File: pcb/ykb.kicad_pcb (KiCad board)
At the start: 2 copper layers, 299.2 x 132.3 mm, 90 parts, among them J1 Conn_01x08_Socket, U1 Helios

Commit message: column trace highway
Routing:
- net col 0: track 95.2 -> 348.7 mm, vias 0 -> 4
- net col 1: track 97.9 -> 297.7 mm, vias 0 -> 4
- net row 0: track 310.3 -> 494.5 mm, vias 20 -> 22
- net col 2: track 96.7 -> 268.2 mm, vias 0 -> 4
- net col 3: track 94.4 -> 230.1 mm, vias 0 -> 4
- net col 4: track 90.5 -> 211.8 mm, vias 0 -> 4
- net col 5: track 86.8 -> 202.0 mm, vias 0 -> 4
- net row 3: track 395.1 -> 338.4 mm, vias 4 -> 2
- net Net-(D21-A): track 0.00 -> 7.78 mm
- net Net-(D22-A): track 0.00 -> 7.68 mm
- net col 6: track 121.8 -> 115.5 mm
- net col 7: track 87.1 -> 81.6 mm
- net col 8: track 89.1 -> 84.9 mm
- net col 9: track 91.3 -> 88.4 mm
- net col 10: track 93.6 -> 91.9 mm

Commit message: fixed incorrect net assignment
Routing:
- net col 11: track 95.0 -> 221.6 mm, vias 0 -> 2
- net col 0: track 348.7 -> 222.1 mm, vias 4 -> 2
- net col 10: track 91.9 -> 193.6 mm, vias 0 -> 2
- net col 1: track 297.7 -> 196.0 mm, vias 4 -> 2
- net col 9: track 88.4 -> 176.5 mm, vias 0 -> 2
- net col 2: track 268.2 -> 180.0 mm, vias 4 -> 2
- net col 3: track 230.1 -> 158.4 mm, vias 4 -> 2
- net col 8: track 84.9 -> 156.6 mm, vias 0 -> 2
- net col 7: track 81.6 -> 135.7 mm, vias 0 -> 2
- net col 4: track 211.8 -> 157.7 mm, vias 4 -> 2
- net col 6: vias 0 -> 1
- net col 5: vias 4 -> 3

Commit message: finished routing
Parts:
- moved D32 4.43 mm to (309.6, 158.7)
- moved J1 2.81 mm to (245.7, 193.2)
- moved U1 1.99 mm to (236.8, 165.9)
- moved S32 1.99 mm to (313.2, 150.0)
- moved D37 1.99 mm to (277.8, 148.9)
- moved S20 1.99 mm to (150.4, 181.2)
- moved D33 1.99 mm to (300.0, 145.0)
- moved D42 1.99 mm to (319.3, 190.4)
- moved S42 1.99 mm to (323.2, 181.2)
- moved D19 1.99 mm to (207.8, 192.9)
- moved S36 1.99 mm to (291.7, 153.1)
- moved S27 1.99 mm to (350.2, 133.9)
- moved D28 1.99 mm to (339.3, 123.9)
- moved D29 1.99 mm to (326.8, 154.4)
- moved D12 1.99 mm to (182.8, 129.4)
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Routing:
- net row 2: track 227.9 -> 544.3 mm, vias 3 -> 24
- net row 1: track 438.2 -> 624.7 mm, vias 23 -> 27
- net row 0: track 494.5 -> 675.0 mm, vias 22 -> 23
- net row 3: track 338.4 -> 513.5 mm, vias 2 -> 6
- net col 8: track 156.6 -> 259.0 mm, vias 2 -> 3
- net col 7: track 135.7 -> 232.5 mm, vias 2 -> 3
- net col 9: track 176.5 -> 271.9 mm, vias 2 -> 3
- net col 3: track 158.4 -> 252.8 mm, vias 2 -> 3
- net col 6: track 115.5 -> 207.3 mm, vias 1 -> 3
- net col 2: track 180.0 -> 270.5 mm, vias 2 -> 3
- net col 4: track 157.7 -> 237.4 mm, vias 2 -> 4
- net col 1: track 196.0 -> 261.9 mm, vias 2 -> 3
- net col 10: track 193.6 -> 256.9 mm, vias 2 -> 3
- net col 11: track 221.6 -> 271.5 mm, vias 2 -> 3
- net col 0: track 222.1 -> 272.0 mm, vias 2 -> 3
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
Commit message: all done other than mounting holes :3
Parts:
- J1: value Conn_01x08_Socket -> Conn_01x07_Socket; footprint Connector_PinHeader_2.54mm:PinHeader_1x08_P2.54mm_Vertical -> Connector_PinHeader_2.54mm:PinHeader_1x07_P2.54mm_Vertical
- moved J1 5.51 mm to (244.5, 198.6)
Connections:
- U1 pad 34: DBL -> unconnected-(U1-P25-Pad34)
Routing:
- net row 2: track 544.3 -> 583.2 mm, vias 24 -> 23
- net DBL: track 17.5 -> 0.00 mm
- net row 1: track 624.7 -> 615.0 mm
- net DDC: track 12.6 -> 18.8 mm
- net DCLK: track 12.6 -> 18.4 mm
- net DDIN: track 12.6 -> 18.4 mm
- net DRST: track 12.6 -> 18.4 mm
- net DCS: track 12.6 -> 18.4 mm
- net 3v3: track 38.8 -> 43.1 mm
- net gnd: track 44.7 -> 49.1 mm
- net col 5: track 206.6 -> 208.2 mm
- net col 1: track 261.9 -> 261.1 mm
- net col 10: track 256.9 -> 256.2 mm
- net col 2: track 270.5 -> 270.0 mm
- net col 4: vias 4 -> 3

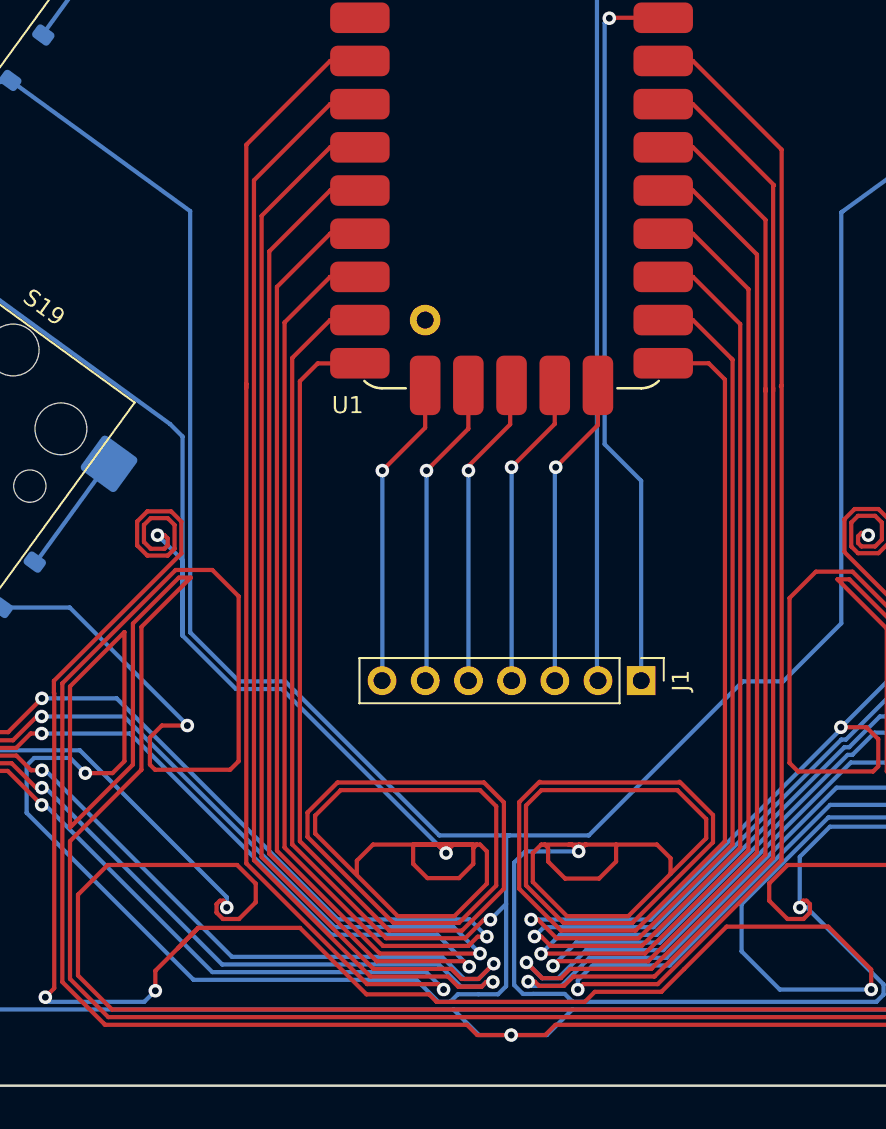
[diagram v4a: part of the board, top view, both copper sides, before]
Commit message: fixed lcd and some design rule errors
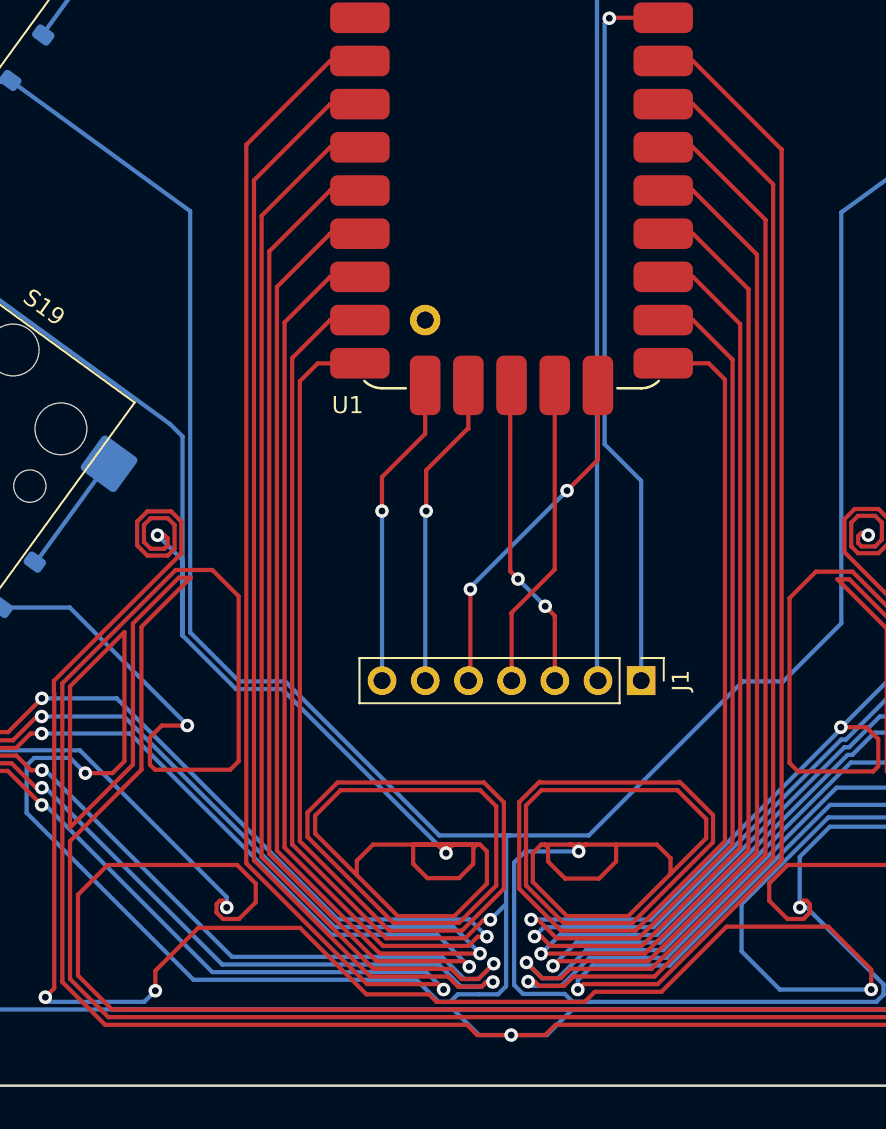
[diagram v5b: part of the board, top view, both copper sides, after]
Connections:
- net DCLK renamed DSDA
- J1 pad 3: DDIN -> DSCL
- J1 pad 5: DCS -> DDC
- J1 pad 6: DDC -> DCS
- U1 pad 26: DDC -> DCS
- U1 pad 27: DCS -> DSCL
- U1 pad 29: DDIN -> DDC
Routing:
- net DSCL: track 0.00 -> 18.5 mm, vias 0 -> 2
- net DDIN: track 18.4 -> 0.00 mm, vias 1 -> 0
- net DDC: track 18.8 -> 20.5 mm, vias 1 -> 2
- net row 1: track 615.0 -> 613.3 mm
- net DSDA: vias 1 -> 0

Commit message: chilled out the routing a little bit lmao
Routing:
- net row 0: track 675.0 -> 442.7 mm, vias 23 -> 25
- net row 1: track 613.3 -> 419.9 mm, vias 27 -> 23
- net row 2: track 583.2 -> 481.1 mm
- net row 3: track 513.5 -> 469.0 mm, vias 6 -> 4
- net Net-(D23-A): track 31.8 -> 29.2 mm
- net Net-(D29-A): track 29.5 -> 26.9 mm

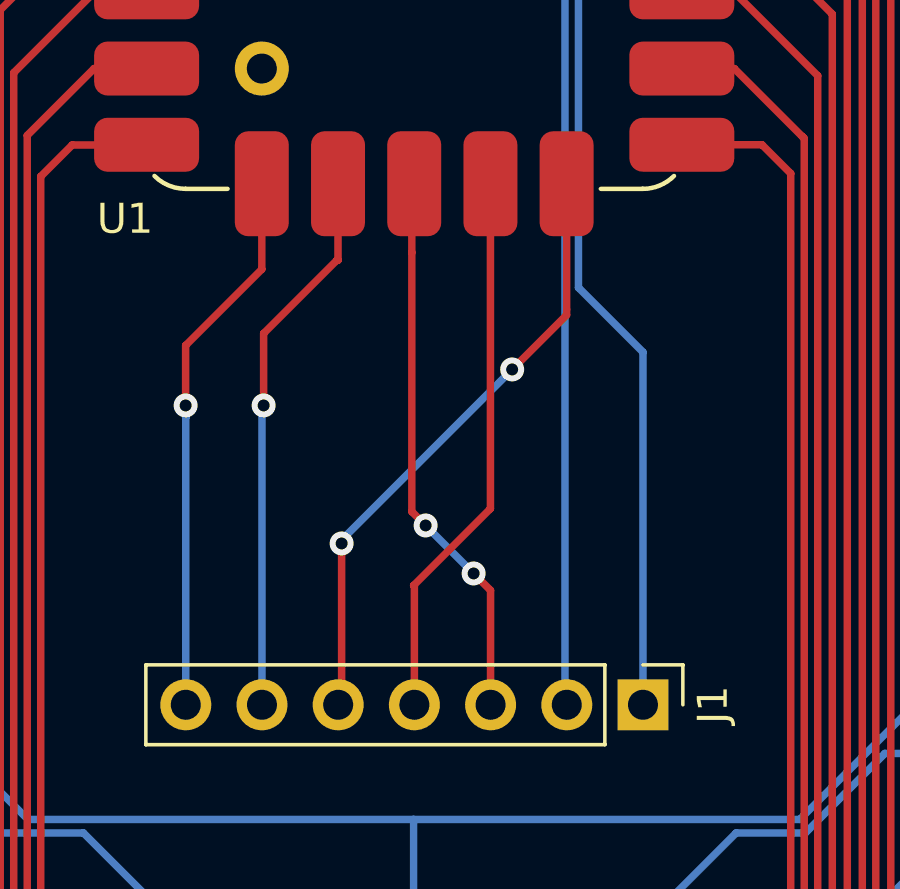
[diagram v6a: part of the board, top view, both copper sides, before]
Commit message: slight touch-up of display tracks
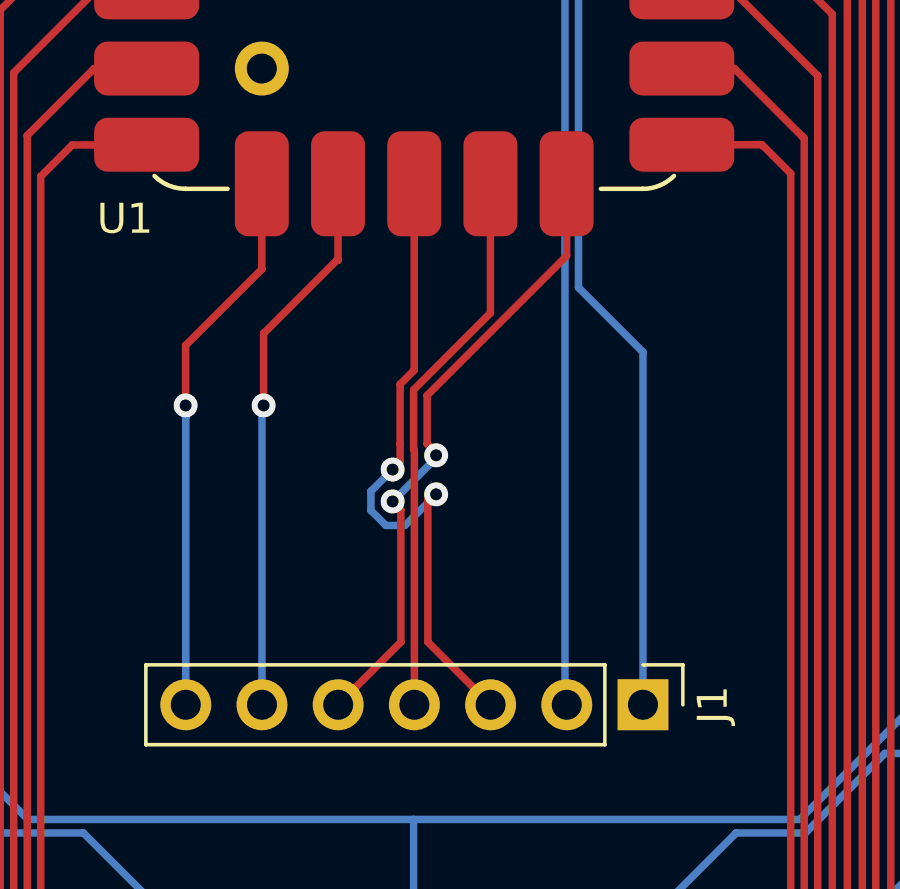
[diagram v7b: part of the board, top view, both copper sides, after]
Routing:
- net DSCL: track 18.5 -> 22.4 mm
- net DDC: track 20.5 -> 21.2 mm
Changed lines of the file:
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@@
+	)
+	(segment
+		(start 237.275 189.880001)
+		(end 237.575002 190.180003)
+		(width 0.25)
+		(layer "F.Cu")
+		(net 73)
+	)
+	(segment
+		(start 241.925005 183.616392)
+		(end 241.925005 181.210008)
+		(width 0.25)
+		(layer "F.Cu")
+		(net 73)
+	)
+	(segment
+		(start 237.275 188.266397)
+		(end 241.925005 183.616392)
+		(width 0.25)
+		(layer "F.Cu")
+		(net 73)
+	)
+	(segment
+		(start 236.400002 192.075)
+		(end 236.400002 196.48773)
+		(width 0.25)
+		(layer "F.Cu")
+		(net 73)
 	)
 	(segment
@@
 	)
 	(segment
-		(start 241.925007 181.210009)
-		(end 241.925007 185.4)
-		(width 0.25)
-		(layer "F.Cu")
-		(net 73)
-	)
-	(segment
-		(start 241.925007 185.585)
-		(end 240.110007 187.4)
-		(width 0.25)
-		(layer "F.Cu")
-		(net 73)
-	)
-	(segment
-		(start 234.425 193.2)
-		(end 234.425 198.462732)
-		(width 0.25)
-		(layer "F.Cu")
-		(net 73)
-	)
-	(segment
-		(start 241.925007 185.4)
-		(end 241.925007 185.585)
-		(width 0.25)
-		(layer "F.Cu")
-		(net 73)
-	)
-	(via
-		(at 234.425 193.2)
-		(size 0.8)
-		(drill 0.4)
-		(layers "F.Cu" "B.Cu")
-		(net 73)
-	)
-	(via
-		(at 240.110007 187.4)
-		(size 0.8)
-		(drill 0.4)
-		(layers "F.Cu" "B.Cu")
-		(net 73)
-	)
-	(segment
-		(start 234.425 193.085007)
-		(end 240.110007 187.4)
-		(width 0.25)
-		(layer "B.Cu")
-		(net 73)
-	)
-	(segment
-		(start 234.425 193.2)
-		(end 234.425 193.085007)
+		(start 237.275 189.880001)
+		(end 237.275 188.266397)
+		(width 0.25)
+		(layer "F.Cu")
+		(net 73)
+	)
+	(segment
+		(start 236.400002 196.48773)
+		(end 234.310002 198.57773)
+		(width 0.25)
+		(layer "F.Cu")
+		(net 73)
+	)
+	(segment
+		(start 236.125002 191.8)
+		(end 236.400002 192.075)
+		(width 0.25)
+		(layer "F.Cu")
+		(net 73)
+	)
+	(segment
+		(start 237.575002 190.180003)
+		(end 237.575002 190.261484)
+		(width 0.25)
+		(layer "F.Cu")
+		(net 73)
+	)
+	(via
+		(at 236.125002 191.8)
+		(size 0.8)
+		(drill 0.4)
+		(layers "F.Cu" "B.Cu")
+		(net 73)
+	)
+	(via
+		(at 237.575002 190.261484)
+		(size 0.8)
+		(drill 0.4)
+		(layers "F.Cu" "B.Cu")
+		(net 73)
+	)
+	(segment
+		(start 237.575002 190.35)
+		(end 237.575002 190.261484)
+		(width 0.25)
+		(layer "B.Cu")
+		(net 73)
+	)
+	(segment
+		(start 236.125002 191.8)
+		(end 237.575002 190.35)
 		(width 0.25)
 		(layer "B.Cu")
@@
 	)
 	(segment
-		(start 239.385007 192.039993)
-		(end 236.825 194.6)
-		(width 0.25)
-		(layer "F.Cu")
-		(net 76)
-	)
-	(segment
-		(start 236.850002 194.625002)
-		(end 236.850002 198.577731)
-		(width 0.25)
-		(layer "F.Cu")
-		(net 76)
-	)
-	(segment
-		(start 236.825 194.6)
-		(end 236.850002 194.625002)
-		(width 0.25)
-		(layer "F.Cu")
-		(net 76)
-	)
-	(segment
-		(start 239.385007 181.210012)
-		(end 239.385007 192.039993)
-		(width 0.25)
-		(layer "F.Cu")
-		(net 76)
-	)
-	(segment
-		(start 236.765016 183.502493)
-		(end 236.765017 181.210014)
-		(width 0.25)
-		(layer "F.Cu")
-		(net 78)
-	)
-	(segment
-		(start 236.765016 192.140016)
-		(end 237.225 192.6)
-		(width 0.25)
-		(layer "F.Cu")
-		(net 78)
-	)
-	(segment
-		(start 238.825 194.2)
-		(end 239.390002 194.765002)
-		(width 0.25)
-		(layer "F.Cu")
-		(net 78)
-	)
-	(segment
-		(start 239.390002 194.765002)
+		(start 236.850002 190.091399)
+		(end 236.825 190.066397)
+		(width 0.25)
+		(layer "F.Cu")
+		(net 76)
+	)
+	(segment
+		(start 236.825 188.080001)
+		(end 239.385003 185.519998)
+		(width 0.25)
+		(layer "F.Cu")
+		(net 76)
+	)
+	(segment
+		(start 236.825 190.066397)
+		(end 236.825 188.080001)
+		(width 0.25)
+		(layer "F.Cu")
+		(net 76)
+	)
+	(segment
+		(start 236.850002 198.577731)
+		(end 236.850002 190.091399)
+		(width 0.25)
+		(layer "F.Cu")
+		(net 76)
+	)
+	(segment
+		(start 239.385003 185.519998)
+		(end 239.385003 181.210004)
+		(width 0.25)
+		(layer "F.Cu")
+		(net 76)
+	)
+	(segment
+		(start 236.375 190.48735)
+		(end 236.125002 190.737348)
+		(width 0.25)
+		(layer "F.Cu")
+		(net 78)
+	)
+	(segment
+		(start 237.462346 191.562654)
+		(end 237.300002 191.724998)
+		(width 0.25)
+		(layer "F.Cu")
+		(net 78)
+	)
+	(segment
+		(start 237.300002 196.48773)
 		(end 239.390002 198.57773)
 		(width 0.25)
@@
 	)
 	(segment
-		(start 236.765016 183.502493)
-		(end 236.765016 192.140016)
-		(width 0.25)
-		(layer "F.Cu")
-		(net 78)
-	)
-	(via
-		(at 237.225 192.6)
-		(size 0.8)
-		(drill 0.4)
-		(layers "F.Cu" "B.Cu")
-		(net 78)
-	)
-	(via
-		(at 238.825 194.2)
-		(size 0.8)
-		(drill 0.4)
-		(layers "F.Cu" "B.Cu")
-		(net 78)
-	)
-	(segment
-		(start 237.225 192.6)
-		(end 238.825 194.2)
-		(width 0.25)
-		(layer "B.Cu")
+		(start 236.845003 181.210007)
+		(end 236.845003 187.423602)
+		(width 0.25)
+		(layer "F.Cu")
+		(net 78)
+	)
+	(segment
+		(start 236.375 189.880001)
+		(end 236.375 190.48735)
+		(width 0.25)
+		(layer "F.Cu")
+		(net 78)
+	)
+	(segment
+		(start 237.300002 191.724998)
+		(end 237.300002 196.48773)
+		(width 0.25)
+		(layer "F.Cu")
+		(net 78)
+	)
+	(segment
+		(start 236.375 187.893605)
+		(end 236.375 189.880001)
+		(width 0.25)
+		(layer "F.Cu")
+		(net 78)
+	)
+	(segment
+		(start 236.845003 187.423602)
+		(end 236.375 187.893605)
+		(width 0.25)
+		(layer "F.Cu")
+		(net 78)
+	)
+	(segment
+		(start 237.575002 191.562654)
+		(end 237.462346 191.562654)
+		(width 0.25)
+		(layer "F.Cu")
+		(net 78)
+	)
+	(via
+		(at 237.575002 191.562654)
+		(size 0.8)
+		(drill 0.4)
+		(layers "F.Cu" "B.Cu")
+		(net 78)
+	)
+	(via
+		(at 236.125002 190.737348)
+		(size 0.8)
+		(drill 0.4)
+		(layers "F.Cu" "B.Cu")
+		(net 78)
+	)
+	(segment
+		(start 236.125002 190.737348)
+		(end 235.400002 191.462348)
+		(width 0.25)
+		(layer "B.Cu")
+		(net 78)
+	)
+	(segment
+		(start 235.899697 192.6)
+		(end 236.537656 192.6)
+		(width 0.25)
+		(layer "B.Cu")
+		(net 78)
+	)
+	(segment
+		(start 235.400002 191.462348)
+		(end 235.400002 192.100305)
+		(width 0.25)
+		(layer "B.Cu")
+		(net 78)
+	)
+	(segment
+		(start 236.537656 192.6)
+		(end 237.575002 191.562654)
+		(width 0.25)
+		(layer "B.Cu")
+		(net 78)
+	)
+	(segment
+		(start 235.400002 192.100305)
+		(end 235.899697 192.6)
+		(width 0.25)
+		(layer "B.Cu")

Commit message: diodes on right side
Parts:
- moved D43 21.9 mm to (308.8, 185.3)
- moved D39 21.7 mm to (281.8, 157.6)
- moved D40 19.9 mm to (271.7, 143.8)
- moved D37 19.6 mm to (284.2, 130.4)
- moved D35 19.6 mm to (304.2, 157.9)
- moved D41 19.5 mm to (272.1, 175.0)
- moved D36 19.4 mm to (294.1, 144.1)
- moved D42 19.3 mm to (325.7, 172.2)
- moved D38 19.3 mm to (291.6, 171.2)
- moved D33 19.0 mm to (307.0, 127.4)
- moved D34 18.6 mm to (298.3, 112.9)
- moved D29 17.9 mm to (334.7, 138.3)
- moved D32 17.9 mm to (315.7, 141.9)
- moved D31 17.6 mm to (319.7, 107.7)
- moved D30 17.0 mm to (327.2, 122.9)
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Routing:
- net Net-(D40-A): track 43.0 -> 7.49 mm
- net row 2: track 481.1 -> 515.5 mm
- net row 3: track 469.0 -> 501.3 mm
- net row 0: track 442.7 -> 470.5 mm, vias 25 -> 27
- net Net-(D37-A): track 33.6 -> 7.44 mm
- net row 1: track 419.9 -> 446.0 mm
- net Net-(D31-A): track 30.8 -> 7.46 mm
- net Net-(D34-A): track 30.3 -> 7.53 mm
- net Net-(D26-A): track 29.3 -> 7.64 mm, vias 2 -> 0
- net Net-(D41-A): track 29.1 -> 7.51 mm
- net Net-(D23-A): track 29.2 -> 7.61 mm
- net Net-(D27-A): track 28.6 -> 7.49 mm, vias 2 -> 0
- net Net-(D39-A): track 28.3 -> 7.64 mm, vias 2 -> 0
- net Net-(D25-A): track 28.0 -> 7.56 mm
- net Net-(D28-A): track 27.7 -> 7.54 mm
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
